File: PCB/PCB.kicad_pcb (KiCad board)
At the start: 4 copper layers, 54 x 29 mm, 111 parts, among them J1 USB_B_Micro, J2 Conn_01x02, Q1 PJA3428, Q2 PJA3428, Q3 AO3401A, SW1 SW_Push, SW2 SW_Push, SW3 SW_Push, SW4 ON/OFF, U1 ESP32-PICO-MINI-02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

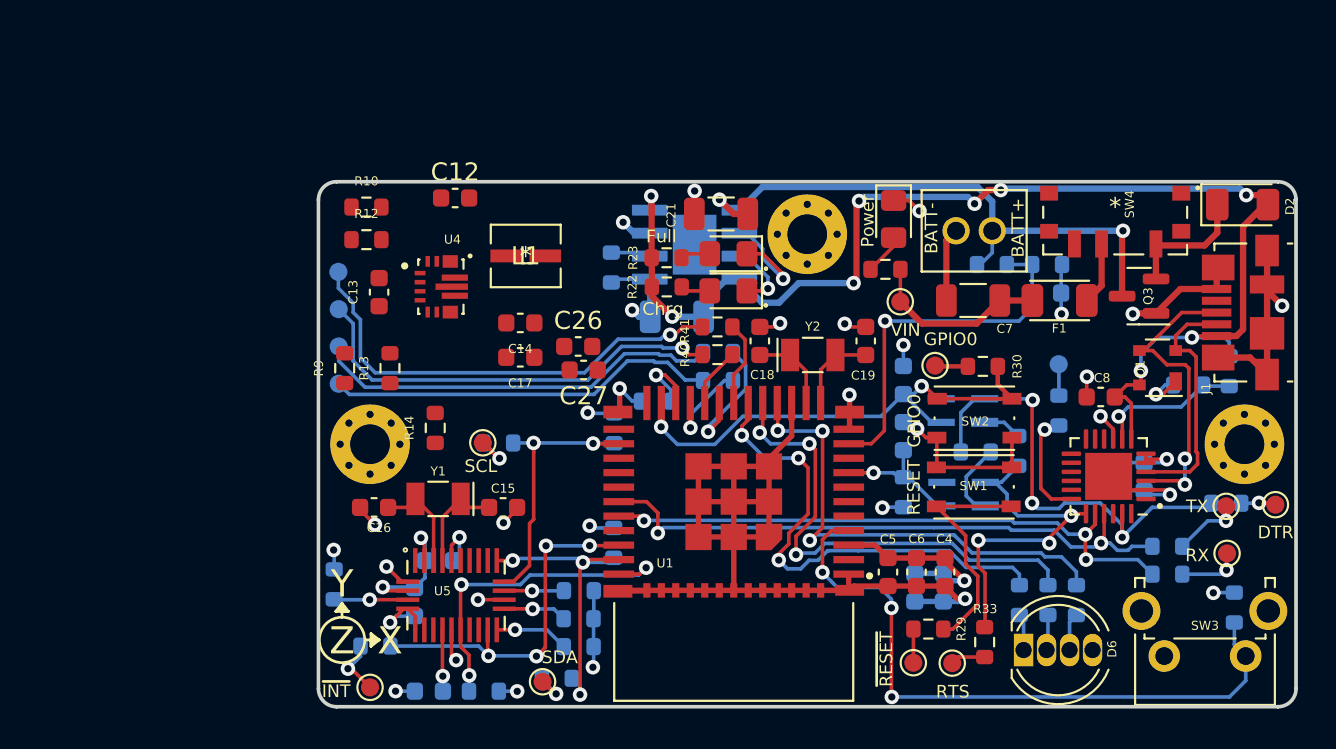
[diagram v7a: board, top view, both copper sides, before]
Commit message: update pcb with Vin input
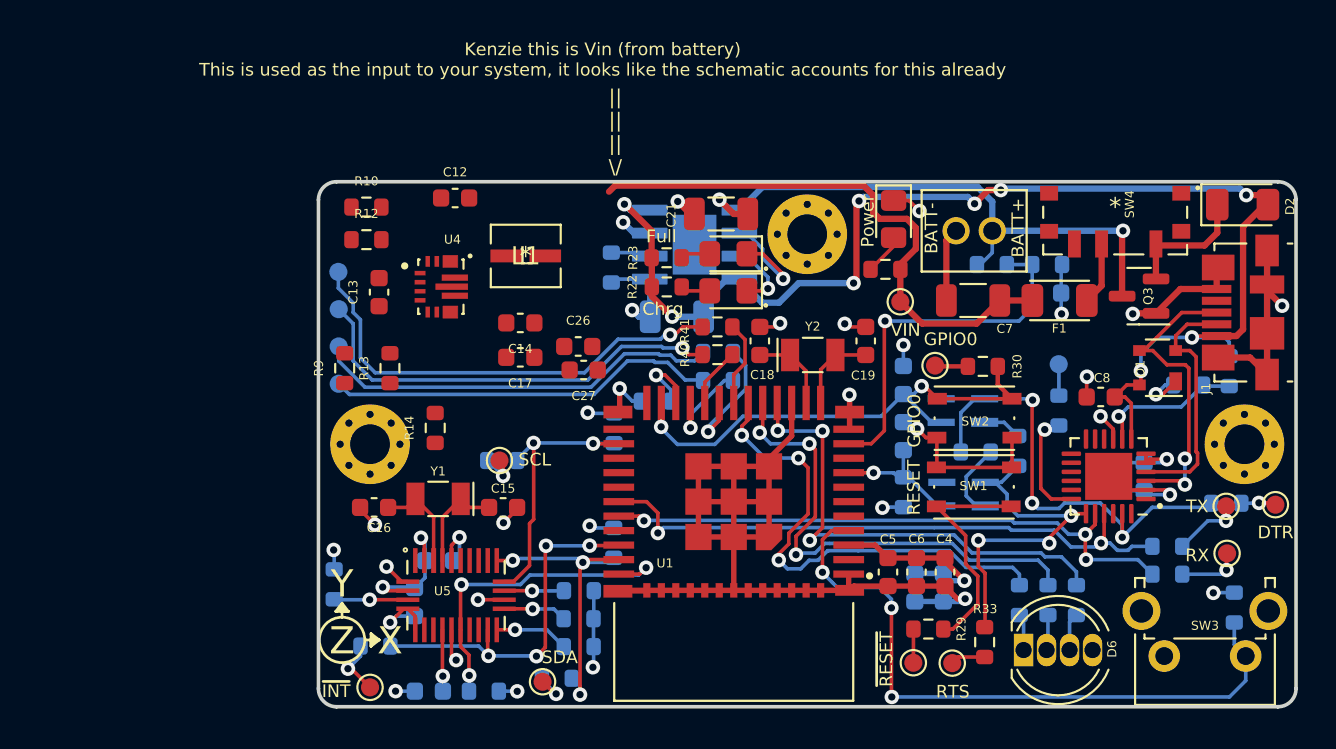
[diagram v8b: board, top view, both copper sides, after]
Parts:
- moved TP14 1.34 mm to (201.7, 106.6)
- moved R37 0.99 mm to (201.8, 106.6)
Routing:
- net Vin: track 10.1 -> 31.4 mm
- net +5V: track 71.6 -> 72.6 mm
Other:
- board text added: "Kenzie this is Vin (from battery) This is used as the input to your system, it looks like the schematic accounts for this already"
- board text added: "|| || || \/"
